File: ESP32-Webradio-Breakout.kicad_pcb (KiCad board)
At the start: 2 copper layers, 80 x 60 mm, 36 parts, among them J1 AudioJack, J2 Conn_01x01, J3 Conn_01x02, Q1 BC547, SW1 RotaryEncoder_Switch, U1 ESP32NodeMCU, U2 PCF8574, U3 DS18B20

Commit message: Rotated display connector by 180 degrees
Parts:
- moved DS1 38.2 mm to (135.8, 46.1), turned to 90 degrees
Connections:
- REF** pad 1: (no net) -> GND
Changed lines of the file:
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@@
     (fp_circle (center 0 0) (end 3.2 0) (layer "Cmts.User") (width 0.15) (fill none))
     (fp_circle (center 0 0) (end 3.45 0) (layer "F.CrtYd") (width 0.05) (fill none))
-    (pad "1" thru_hole circle (at 0 0 90) (size 6.4 6.4) (drill 3.2) (layers *.Cu *.Mask))
+    (pad "1" thru_hole circle (at 0 0 90) (size 6.4 6.4) (drill 3.2) (layers *.Cu *.Mask)
+      (net 9 "GND"))
   )
   (footprint "Resistor_THT:R_Axial_DIN0207_L6.3mm_D2.5mm_P10.16mm_Horizontal" (layer "F.Cu")
@@
   )
   (footprint "Connector_PinHeader_2.54mm:PinHeader_1x16_P2.54mm_Vertical" (layer "F.Cu")
-    (at 174.005 46.1 -90)
+    (at 135.8 46.1 90)
     (descr "Through hole straight pin header, 1x16, 2.54mm pitch, single row")
     (tags "Through hole pin header THT 1x16 2.54mm single row")
@@
     (property "Sheetname" "")
     (attr through_hole)
-    (fp_text reference "DS1" (at 2.125 25.83) (layer "F.SilkS")
+    (fp_text reference "DS1" (at -2.1 12.9) (layer "F.SilkS")
       (effects (font (size 1 1) (thickness 0.15)))
     )
@@
     (fp_line (start 1.27 39.37) (end -1.27 39.37) (layer "F.Fab") (width 0.1))
     (fp_line (start -0.635 -1.27) (end 1.27 -1.27) (layer "F.Fab") (width 0.1))
-    (pad "1" thru_hole rect (at 0 0 270) (size 1.7 1.7) (drill 1) (layers *.Cu *.Mask)
+    (pad "1" thru_hole rect (at 0 0 90) (size 1.7 1.7) (drill 1) (layers *.Cu *.Mask)
       (net 9 "GND") (pinfunction "VSS") (pintype "power_in"))
-    (pad "2" thru_hole oval (at 0 2.54 270) (size 1.7 1.7) (drill 1) (layers *.Cu *.Mask)
+    (pad "2" thru_hole oval (at 0 2.54 90) (size 1.7 1.7) (drill 1) (layers *.Cu *.Mask)
       (net 10 "+5V") (pinfunction "VDD") (pintype "power_in"))
-    (pad "3" thru_hole oval (at 0 5.08 270) (size 1.7 1.7) (drill 1) (layers *.Cu *.Mask)
+    (pad "3" thru_hole oval (at 0 5.08 90) (size 1.7 1.7) (drill 1) (layers *.Cu *.Mask)
       (net 13 "Net-(DS1-Pad3)") (pinfunction "VO") (pintype "input"))
-    (pad "4" thru_hole oval (at 0 7.62 270) (size 1.7 1.7) (drill 1) (layers *.Cu *.Mask)
+    (pad "4" thru_hole oval (at 0 7.62 90) (size 1.7 1.7) (drill 1) (layers *.Cu *.Mask)
       (net 42 "/P0") (pinfunction "RS") (pintype "input"))
-    (pad "5" thru_hole oval (at 0 10.16 270) (size 1.7 1.7) (drill 1) (layers *.Cu *.Mask)
+    (pad "5" thru_hole oval (at 0 10.16 90) (size 1.7 1.7) (drill 1) (layers *.Cu *.Mask)
       (net 14 "Net-(DS1-Pad5)") (pinfunction "R/W") (pintype "input"))
-    (pad "6" thru_hole oval (at 0 12.7 270) (size 1.7 1.7) (drill 1) (layers *.Cu *.Mask)
+    (pad "6" thru_hole oval (at 0 12.7 90) (size 1.7 1.7) (drill 1) (layers *.Cu *.Mask)
       (net 43 "/P2") (pinfunction "E") (pintype "input"))
-    (pad "7" thru_hole oval (at 0 15.24 270) (size 1.7 1.7) (drill 1) (layers *.Cu *.Mask)
+    (pad "7" thru_hole oval (at 0 15.24 90) (size 1.7 1.7) (drill 1) (layers *.Cu *.Mask)
       (net 44 "unconnected-(DS1-Pad7)") (pinfunction "D0") (pintype "input+no_connect"))
-    (pad "8" thru_hole oval (at 0 17.78 270) (size 1.7 1.7) (drill 1) (layers *.Cu *.Mask)
+    (pad "8" thru_hole oval (at 0 17.78 90) (size 1.7 1.7) (drill 1) (layers *.Cu *.Mask)
       (net 45 "unconnected-(DS1-Pad8)") (pinfunction "D1") (pintype "input+no_connect"))
-    (pad "9" thru_hole oval (at 0 20.32 270) (size 1.7 1.7) (drill 1) (layers *.Cu *.Mask)
+    (pad "9" thru_hole oval (at 0 20.32 90) (size 1.7 1.7) (drill 1) (layers *.Cu *.Mask)
       (net 46 "unconnected-(DS1-Pad9)") (pinfunction "D2") (pintype "input+no_connect"))
-    (pad "10" thru_hole oval (at 0 22.86 270) (size 1.7 1.7) (drill 1) (layers *.Cu *.Mask)
+    (pad "10" thru_hole oval (at 0 22.86 90) (size 1.7 1.7) (drill 1) (layers *.Cu *.Mask)
       (net 47 "unconnected-(DS1-Pad10)") (pinfunction "D3") (pintype "input+no_connect"))
-    (pad "11" thru_hole oval (at 0 25.4 270) (size 1.7 1.7) (drill 1) (layers *.Cu *.Mask)
+    (pad "11" thru_hole oval (at 0 25.4 90) (size 1.7 1.7) (drill 1) (layers *.Cu *.Mask)
       (net 15 "Net-(DS1-Pad11)") (pinfunction "D4") (pintype "input"))
-    (pad "12" thru_hole oval (at 0 27.94 270) (size 1.7 1.7) (drill 1) (layers *.Cu *.Mask)
+    (pad "12" thru_hole oval (at 0 27.94 90) (size 1.7 1.7) (drill 1) (layers *.Cu *.Mask)
       (net 19 "Net-(DS1-Pad12)") (pinfunction "D5") (pintype "input"))
-    (pad "13" thru_hole oval (at 0 30.48 270) (size 1.7 1.7) (drill 1) (layers *.Cu *.Mask)
+    (pad "13" thru_hole oval (at 0 30.48 90) (size 1.7 1.7) (drill 1) (layers *.Cu *.Mask)
       (net 21 "Net-(DS1-Pad13)") (pinfunction "D6") (pintype "input"))
-    (pad "14" thru_hole oval (at 0 33.02 270) (size 1.7 1.7) (drill 1) (layers *.Cu *.Mask)
+    (pad "14" thru_hole oval (at 0 33.02 90) (size 1.7 1.7) (drill 1) (layers *.Cu *.Mask)
       (net 22 "Net-(DS1-Pad14)") (pinfunction "D7") (pintype "input"))
-    (pad "15" thru_hole oval (at 0 35.56 270) (size 1.7 1.7) (drill 1) (layers *.Cu *.Mask)
+    (pad "15" thru_hole oval (at 0 35.56 90) (size 1.7 1.7) (drill 1) (layers *.Cu *.Mask)
       (net 10 "+5V") (pinfunction "LED(+)") (pintype "power_in"))
-    (pad "16" thru_hole oval (at 0 38.1 270) (size 1.7 1.7) (drill 1) (layers *.Cu *.Mask)
+    (pad "16" thru_hole oval (at 0 38.1 90) (size 1.7 1.7) (drill 1) (layers *.Cu *.Mask)
       (net 23 "Net-(DS1-Pad16)") (pinfunction "LED(-)") (pintype "power_in"))
     (model "${KICAD6_3DMODEL_DIR}/Connector_PinHeader_2.54mm.3dshapes/PinHeader_1x16_P2.54mm_Vertical.wrl"

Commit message: routing first tracks
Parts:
- moved R11 1.23 mm to (170.7, 86.9)
- moved R12 1.23 mm to (173.8, 86.9)
- moved R16 1.23 mm to (136.9, 76.7)
- moved R4 1.23 mm to (149.2, 76.7)
- moved R6 1.23 mm to (155.4, 86.9)
- moved R7 1.23 mm to (158.4, 86.9)
- moved R1 1.23 mm to (139.9, 86.9)
- moved R10 1.23 mm to (167.7, 86.9)
- moved R2 1.23 mm to (143.1, 86.9)
- moved R3 1.23 mm to (146.2, 86.9)
- moved R5 1.23 mm to (152.3, 76.7)
- moved R8 1.23 mm to (161.5, 86.9)
- moved R9 1.23 mm to (164.6, 86.9)
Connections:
- J3 pad 2: /SDA -> /SCL
- R9 pad 2: /SDA -> /SCL
- U1 pad 33: /SDA -> /SCL
- U2 pad 15: /SDA -> /SCL
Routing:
- net +5V: track 0.00 -> 222.6 mm, vias 0 -> 1
- net +3V3: track 0.00 -> 167.7 mm
- net /SCL: track 0.00 -> 112.7 mm, vias 0 -> 2
- net Net-(C2-Pad1): track 0.00 -> 102.0 mm
- net Net-(C1-Pad1): track 0.00 -> 98.3 mm
- net /Audio_R: track 0.00 -> 83.3 mm
- net /Audio_L: track 0.00 -> 76.9 mm, vias 0 -> 1
- net /LCD_Dimm: track 0.00 -> 58.6 mm
- net /P2: track 0.00 -> 40.0 mm, vias 0 -> 1
- net Net-(DS1-Pad5): track 0.00 -> 39.0 mm, vias 0 -> 1
- net /P0: track 0.00 -> 38.8 mm, vias 0 -> 1
- net /Light_Sens: track 0.00 -> 31.4 mm
- net Net-(DS1-Pad11): track 0.00 -> 28.8 mm, vias 0 -> 1
- net Net-(DS1-Pad12): track 0.00 -> 26.1 mm, vias 0 -> 1
- net Net-(DS1-Pad13): track 0.00 -> 23.3 mm, vias 0 -> 1
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
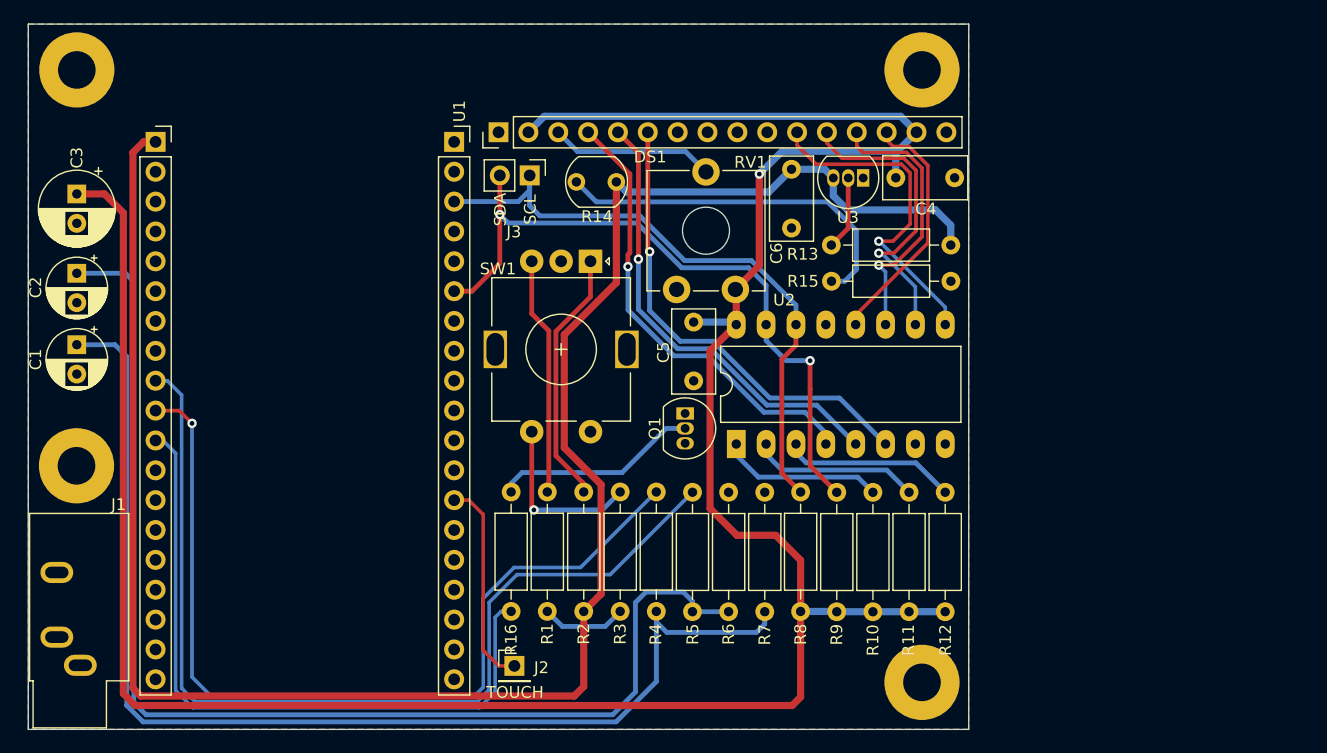
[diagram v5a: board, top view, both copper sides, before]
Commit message: Added MicroSD cardreader
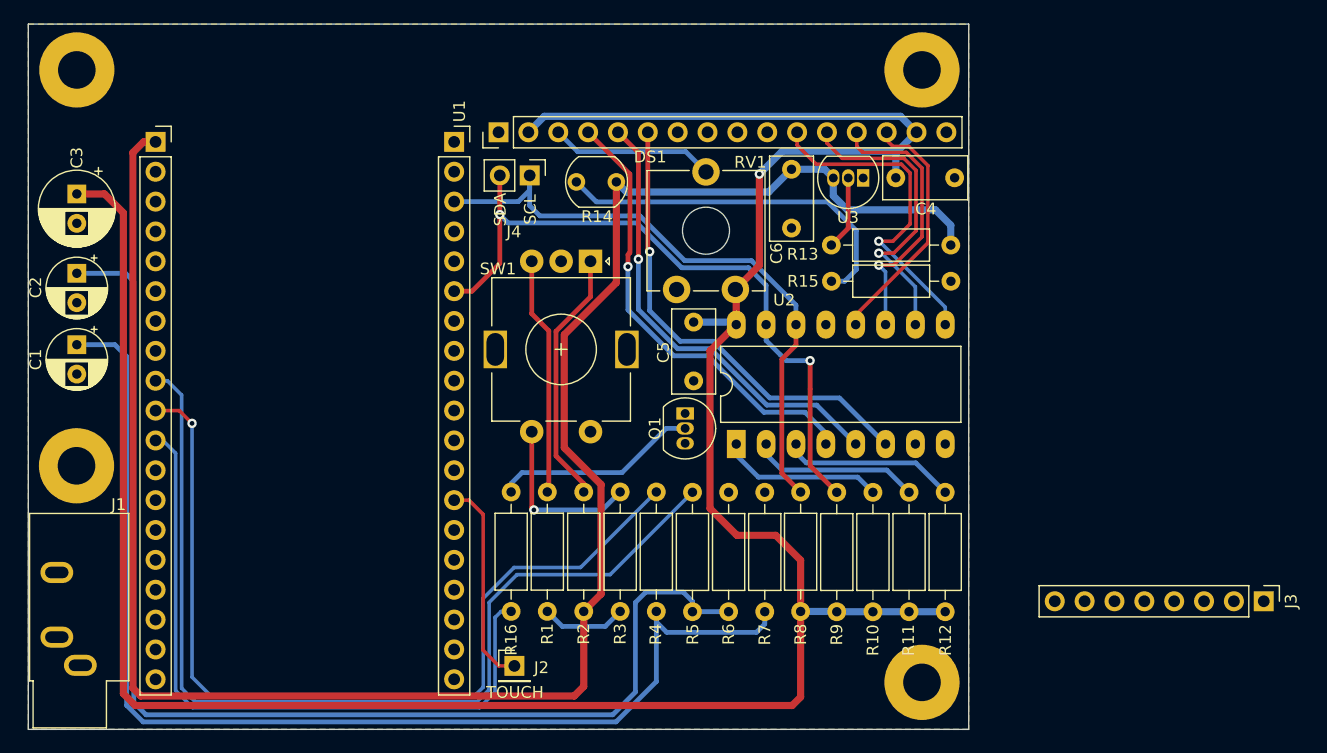
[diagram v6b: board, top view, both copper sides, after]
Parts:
- added J3: Micro_SD_Card, Connector_PinHeader_2.54mm:PinHeader_1x08_P2.54mm_Vertical, F.Cu at (200.9, 86.0)
- renumbered J3 to J4
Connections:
- J4 pad 2: /SCL -> /SDA
- R9 pad 2: /SCL -> /SDA
- U1 pad 33: /SCL -> /SDA
- U2 pad 15: /SCL -> /SDA
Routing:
- net /SDA: track 0.00 -> 58.8 mm, vias 0 -> 2
- net /SCL: track 112.7 -> 53.9 mm, vias 2 -> 0

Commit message: everything routed the first time, some ground connections still need to be done properly.
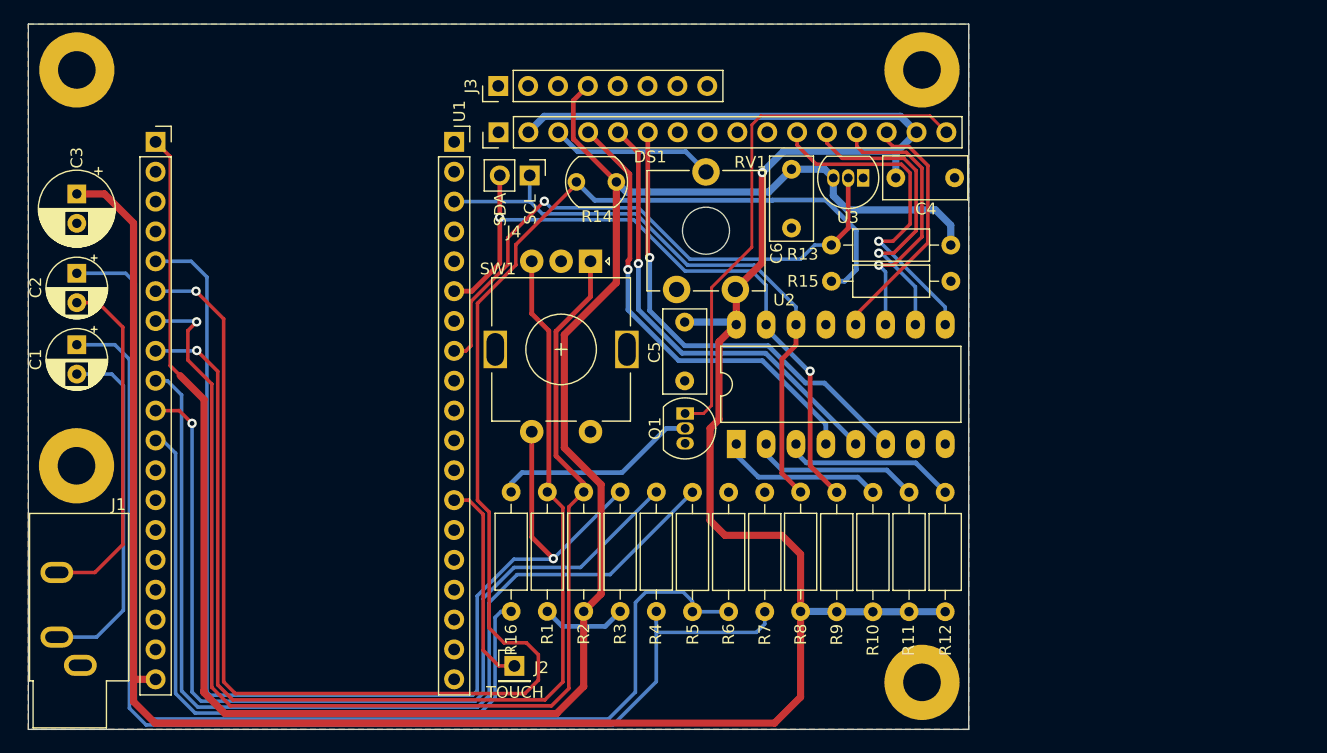
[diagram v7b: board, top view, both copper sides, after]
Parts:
- moved J3 78.5 mm to (135.8, 42.2), turned to 90 degrees
- moved C5 0.76 mm to (151.6, 62.2)
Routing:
- net /Light_Sens: track 31.4 -> 145.8 mm, vias 0 -> 1
- net /Enc_A: track 21.8 -> 106.7 mm, vias 0 -> 1
- net /Enc_SW: track 14.7 -> 98.9 mm
- net /Enc_B: track 20.3 -> 100.2 mm, vias 0 -> 1
- net Net-(DS1-Pad16): track 0.00 -> 45.3 mm
- net /Temp_Sens: track 6.30 -> 49.7 mm, vias 0 -> 1
- net Net-(C1-Pad2): track 0.00 -> 30.1 mm
- net Net-(C2-Pad2): track 0.00 -> 29.9 mm
- net +3V3: track 167.7 -> 173.6 mm
- net +5V: track 222.6 -> 226.4 mm
- net /SCL: track 53.9 -> 51.9 mm
- net /Audio_L: track 76.9 -> 78.3 mm
- net /SDA: track 58.8 -> 57.6 mm
- net /LCD_Dimm: track 58.6 -> 59.4 mm
- net /Audio_R: track 83.3 -> 84.1 mm

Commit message: changing value of R6 and R7 to 22k. moving some tracks nicely
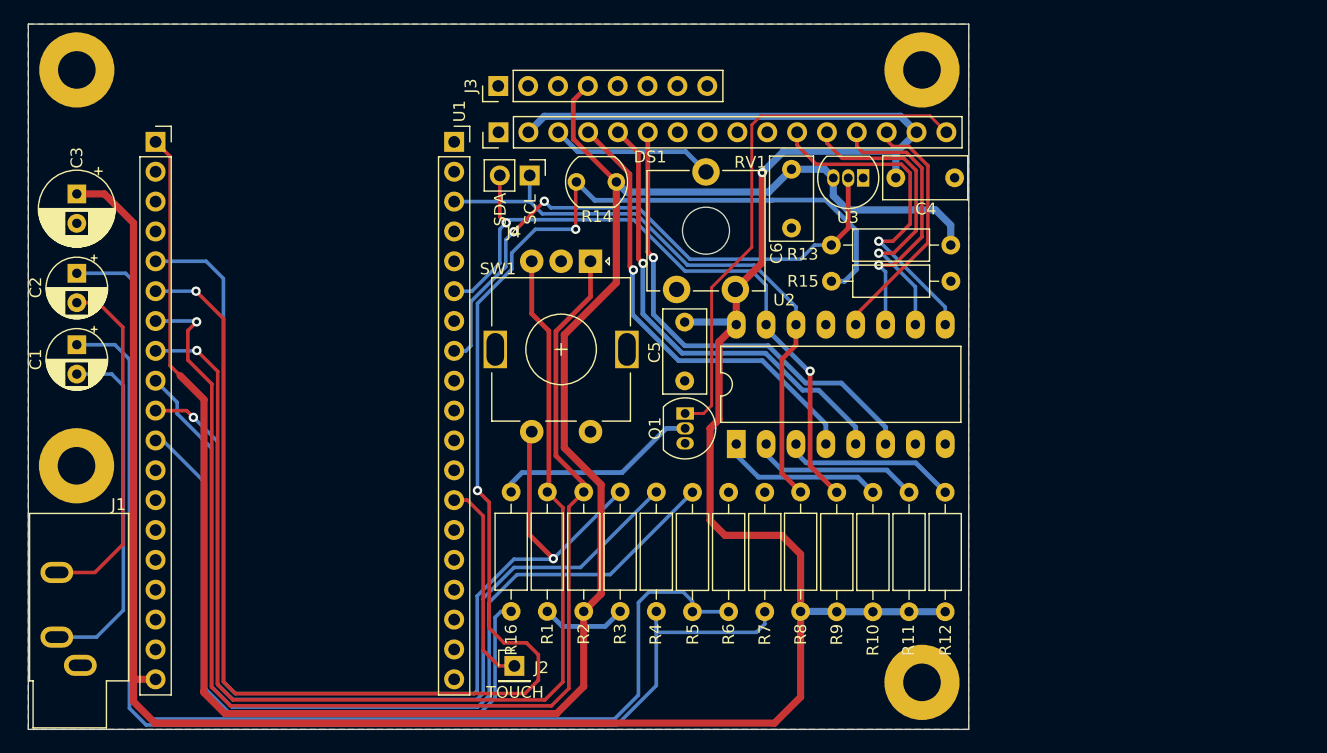
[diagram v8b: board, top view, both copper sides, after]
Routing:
- net /Audio_R: track 84.1 -> 81.8 mm
- net /Light_Sens: track 145.8 -> 147.9 mm, vias 1 -> 3
- net /LCD_Dimm: track 59.4 -> 57.7 mm
- net /Audio_L: track 78.3 -> 76.9 mm
- net /P2: track 40.0 -> 40.9 mm
- net Net-(DS1-Pad5): track 39.1 -> 39.9 mm
- net /Enc_SW: track 98.9 -> 98.4 mm
- net /Temp_Sens: vias 1 -> 2
